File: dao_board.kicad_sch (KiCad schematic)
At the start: 44 parts, among them J1 DISH_LED, J10 KEY6, J11 KEY7, J12 START, J13 SELECT, J14 DISH_SENSOR, J2 USB_C, J3 SWD, J4 GPIO_EXPANSION, J5 KEY1, J6 KEY2, J7 KEY3, J8 KEY4, J9 KEY5, SW1 HX 3x4x2-2P-1.6N, SW2 RESET, U1 MDBT50Q-1MV2, U2 TLC6C598PWR, U3 TLC6C598PWR

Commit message: 回路図の自動アノテーションのやり直し
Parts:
- renumbered C5 to C3, C6 to C4, C3 to C5, C4 to C6, SW2 to SW1, SW1 to SW2
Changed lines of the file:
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@@
 		(dnp no)
 		(fields_autoplaced yes)
-		(property "Reference" "#PWR07"
+		(property "Reference" "#PWR06"
 			(at 45.72 166.37 0)
 			(hide yes)
@@
 			(project "dao_board"
 				(path "/88e2b3bc-f15b-46e0-bc23-bfcd5e24d1de"
-					(reference "#PWR07")
+					(reference "#PWR06")
 					(unit 1)
 				)
@@
 		(dnp no)
 		(fields_autoplaced yes)
-		(property "Reference" "#PWR021"
+		(property "Reference" "#PWR027"
 			(at 247.65 87.63 0)
 			(hide yes)
@@
 			(project "dao_board"
 				(path "/88e2b3bc-f15b-46e0-bc23-bfcd5e24d1de"
-					(reference "#PWR021")
+					(reference "#PWR027")
 					(unit 1)
 				)
@@
 		(in_pos_files yes)
 		(dnp no)
-		(property "Reference" "C5"
+		(property "Reference" "C3"
 			(at 191.008 101.854 90)
 			(show_name no)
@@
 			(project "dao_board"
 				(path "/88e2b3bc-f15b-46e0-bc23-bfcd5e24d1de"
-					(reference "C5")
+					(reference "C3")
 					(unit 1)
 				)
@@
 		(dnp no)
 		(fields_autoplaced yes)
-		(property "Reference" "#PWR025"
+		(property "Reference" "#PWR024"
 			(at 238.76 109.22 0)
 			(hide yes)
@@
 			(project "dao_board"
 				(path "/88e2b3bc-f15b-46e0-bc23-bfcd5e24d1de"
-					(reference "#PWR025")
+					(reference "#PWR024")
 					(unit 1)
 				)
@@
 		(dnp no)
 		(fields_autoplaced yes)
-		(property "Reference" "SW1"
+		(property "Reference" "SW2"
 			(at 63.5 63.1825 0)
 			(show_name no)
@@
 			(project "dao_board"
 				(path "/88e2b3bc-f15b-46e0-bc23-bfcd5e24d1de"
-					(reference "SW1")
+					(reference "SW2")
 					(unit 1)
 				)
@@
 		(dnp no)
 		(fields_autoplaced yes)
-		(property "Reference" "#PWR05"
+		(property "Reference" "#PWR011"
 			(at 74.93 71.12 0)
 			(hide yes)
@@
 			(project "dao_board"
 				(path "/88e2b3bc-f15b-46e0-bc23-bfcd5e24d1de"
-					(reference "#PWR05")
+					(reference "#PWR011")
 					(unit 1)
 				)
@@
 		(dnp no)
 		(fields_autoplaced yes)
-		(property "Reference" "#PWR027"
+		(property "Reference" "#PWR021"
 			(at 173.99 102.87 0)
 			(hide yes)
@@
 			(project "dao_board"
 				(path "/88e2b3bc-f15b-46e0-bc23-bfcd5e24d1de"
-					(reference "#PWR027")
+					(reference "#PWR021")
 					(unit 1)
 				)
@@
 		(dnp no)
 		(fields_autoplaced yes)
-		(property "Reference" "#PWR029"
+		(property "Reference" "#PWR019"
 			(at 172.72 127 0)
 			(hide yes)
@@
 			(project "dao_board"
 				(path "/88e2b3bc-f15b-46e0-bc23-bfcd5e24d1de"
-					(reference "#PWR029")
+					(reference "#PWR019")
 					(unit 1)
 				)
@@
 		(in_pos_files yes)
 		(dnp no)
-		(property "Reference" "C4"
+		(property "Reference" "C6"
 			(at 237.49 96.774 90)
 			(show_name no)
@@
 			(project "dao_board"
 				(path "/88e2b3bc-f15b-46e0-bc23-bfcd5e24d1de"
-					(reference "C4")
+					(reference "C6")
 					(unit 1)
 				)
@@
 		(dnp no)
 		(fields_autoplaced yes)
-		(property "Reference" "#PWR024"
+		(property "Reference" "#PWR030"
 			(at 265.43 78.74 0)
 			(hide yes)
@@
 			(project "dao_board"
 				(path "/88e2b3bc-f15b-46e0-bc23-bfcd5e24d1de"
-					(reference "#PWR024")
+					(reference "#PWR030")
 					(unit 1)
 				)
@@
 		(dnp no)
 		(fields_autoplaced yes)
-		(property "Reference" "C3"
+		(property "Reference" "C5"
 			(at 237.49 80.01 90)
 			(show_name no)
@@
 			(project "dao_board"
 				(path "/88e2b3bc-f15b-46e0-bc23-bfcd5e24d1de"
-					(reference "C3")
+					(reference "C5")
 					(unit 1)
 				)
@@
 		(dnp no)
 		(fields_autoplaced yes)
-		(property "Reference" "#PWR012"
+		(property "Reference" "#PWR07"
 			(at 50.8 111.76 0)
 			(hide yes)
@@
 			(project "dao_board"
 				(path "/88e2b3bc-f15b-46e0-bc23-bfcd5e24d1de"
-					(reference "#PWR012")
+					(reference "#PWR07")
 					(unit 1)
 				)
@@
 		(dnp no)
 		(fields_autoplaced yes)
-		(property "Reference" "#PWR022"
+		(property "Reference" "#PWR028"
 			(at 247.65 92.71 0)
 			(hide yes)
@@
 			(project "dao_board"
 				(path "/88e2b3bc-f15b-46e0-bc23-bfcd5e24d1de"
-					(reference "#PWR022")
+					(reference "#PWR028")
 					(unit 1)
 				)
@@
 		(dnp no)
 		(fields_autoplaced yes)
-		(property "Reference" "#PWR020"
+		(property "Reference" "#PWR026"
 			(at 241.3 54.61 0)
 			(hide yes)
@@
 			(project "dao_board"
 				(path "/88e2b3bc-f15b-46e0-bc23-bfcd5e24d1de"
-					(reference "#PWR020")
+					(reference "#PWR026")
 					(unit 1)
 				)
@@
 		(dnp no)
 		(fields_autoplaced yes)
-		(property "Reference" "#PWR06"
+		(property "Reference" "#PWR05"
 			(at 41.91 148.59 0)
 			(hide yes)
@@
 			(project "dao_board"
 				(path "/88e2b3bc-f15b-46e0-bc23-bfcd5e24d1de"
-					(reference "#PWR06")
+					(reference "#PWR05")
 					(unit 1)
 				)
@@
 		(dnp no)
 		(fields_autoplaced yes)
-		(property "Reference" "#PWR028"
+		(property "Reference" "#PWR022"
 			(at 173.99 134.62 0)
 			(hide yes)
@@
 			(project "dao_board"
 				(path "/88e2b3bc-f15b-46e0-bc23-bfcd5e24d1de"
-					(reference "#PWR028")
+					(reference "#PWR022")
 					(unit 1)
 				)
@@
 		(in_pos_files yes)
 		(dnp no)
-		(property "Reference" "C6"
+		(property "Reference" "C4"
 			(at 191.008 133.858 90)
 			(show_name no)
@@
 			(project "dao_board"
 				(path "/88e2b3bc-f15b-46e0-bc23-bfcd5e24d1de"
-					(reference "C6")
+					(reference "C4")
 					(unit 1)
 				)
@@
 		(dnp no)
 		(fields_autoplaced yes)
-		(property "Reference" "#PWR011"
+		(property "Reference" "#PWR012"
 			(at 69.85 53.34 0)
 			(hide yes)
@@
 			(project "dao_board"
 				(path "/88e2b3bc-f15b-46e0-bc23-bfcd5e24d1de"
-					(reference "#PWR011")
+					(reference "#PWR012")
 					(unit 1)
 				)
@@
 		(dnp no)
 		(fields_autoplaced yes)
-		(property "Reference" "#PWR023"
+		(property "Reference" "#PWR029"
 			(at 275.59 43.18 0)
 			(hide yes)
@@
 			(project "dao_board"
 				(path "/88e2b3bc-f15b-46e0-bc23-bfcd5e24d1de"
-					(reference "#PWR023")
+					(reference "#PWR029")
 					(unit 1)
 				)
@@
 		(dnp no)
 		(fields_autoplaced yes)
-		(property "Reference" "#PWR030"
+		(property "Reference" "#PWR020"
 			(at 172.72 158.75 0)
 			(hide yes)
@@
 			(project "dao_board"
 				(path "/88e2b3bc-f15b-46e0-bc23-bfcd5e24d1de"
-					(reference "#PWR030")
+					(reference "#PWR020")
 					(unit 1)
 				)
@@
 		(dnp no)
 		(fields_autoplaced yes)
-		(property "Reference" "#PWR026"
+		(property "Reference" "#PWR025"
 			(at 238.76 140.97 0)
 			(hide yes)
@@
 			(project "dao_board"
 				(path "/88e2b3bc-f15b-46e0-bc23-bfcd5e24d1de"
-					(reference "#PWR026")
+					(reference "#PWR025")
 					(unit 1)
 				)
@@
 		(dnp no)
 		(fields_autoplaced yes)
-		(property "Reference" "#PWR019"
+		(property "Reference" "#PWR023"
 			(at 223.52 54.61 0)
 			(hide yes)
@@
 			(project "dao_board"
 				(path "/88e2b3bc-f15b-46e0-bc23-bfcd5e24d1de"
-					(reference "#PWR019")
+					(reference "#PWR023")
 					(unit 1)
 				)
@@
 		(dnp no)
 		(fields_autoplaced yes)
-		(property "Reference" "SW2"
+		(property "Reference" "SW1"
 			(at 39.37 104.14 0)
 			(show_name no)
@@
 			(project "dao_board"
 				(path "/88e2b3bc-f15b-46e0-bc23-bfcd5e24d1de"
-					(reference "SW2")
+					(reference "SW1")
 					(unit 1)
 				)

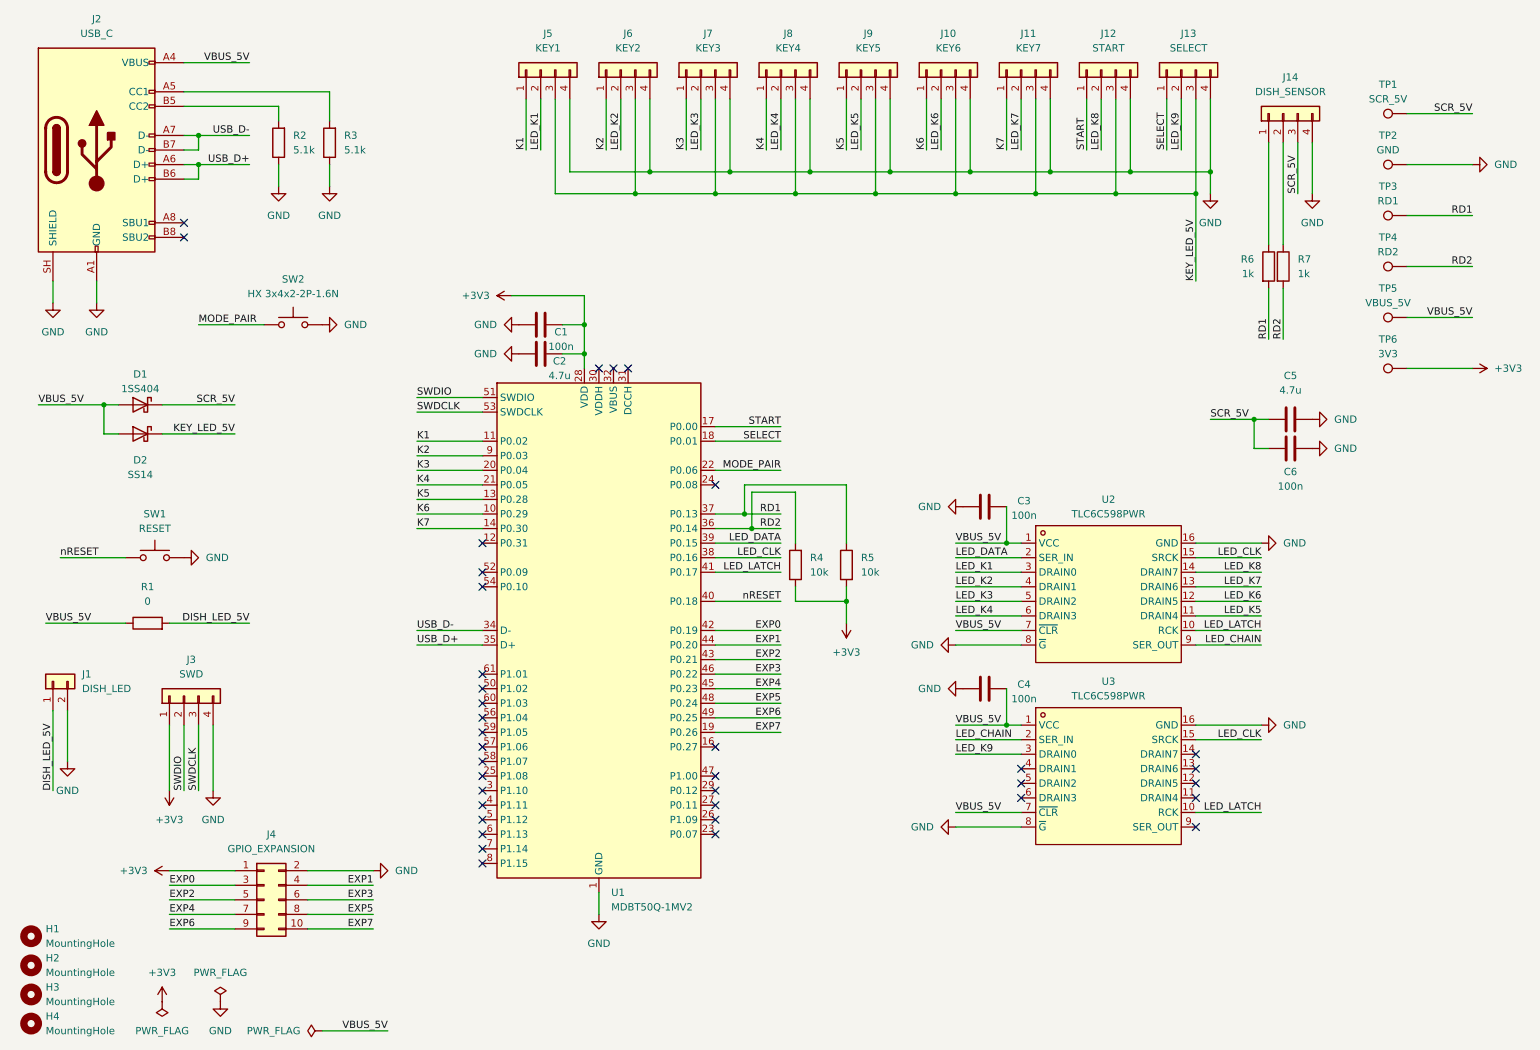
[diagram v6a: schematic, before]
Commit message: USB_Cのシンボルとフットプリントにxiがあったのでシンボル側を適合させた
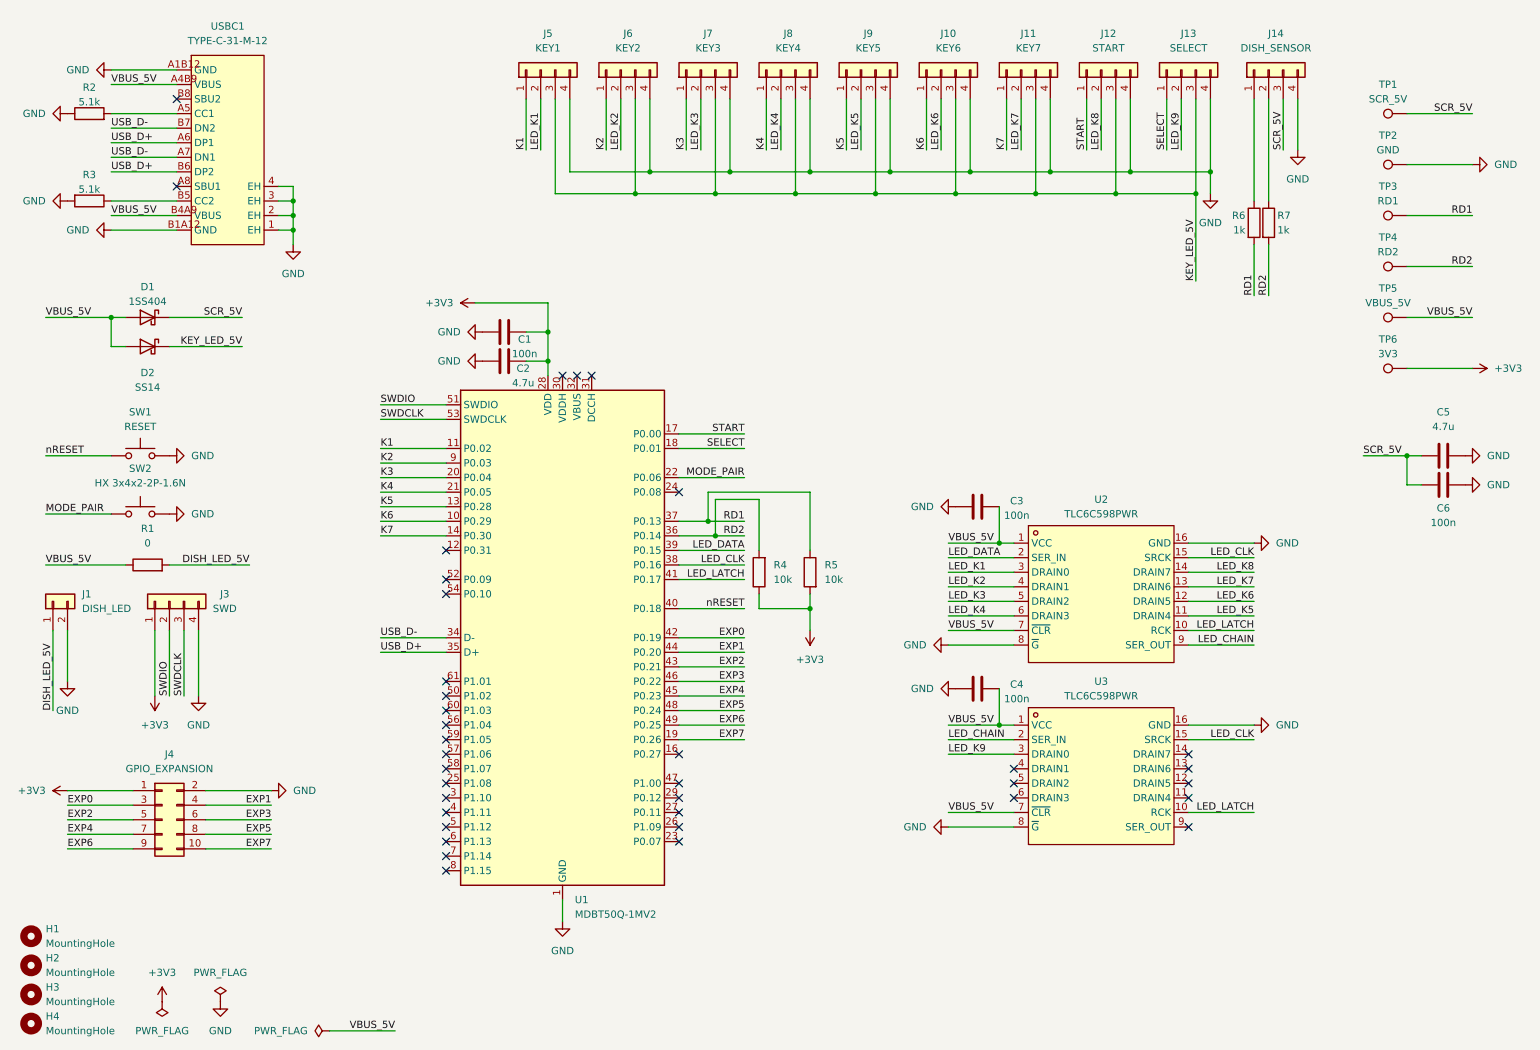
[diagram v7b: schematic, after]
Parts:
- removed J2: USB_C, c165948:USB-C_SMD-TYPE-C-31-M-12_1, symbol Connector:USB_C_Receptacle_USB2.0_16P
- added USBC1: TYPE-C-31-M-12, a:USB-C_SMD-TYPE-C-31-M-12_1, symbol c165948:TYPE-C-31-M-12
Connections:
- net GND: now also R3.2, USBC1.1 (EH), USBC1.2 (EH), USBC1.3 (EH), USBC1.4 (EH), USBC1.A1B12 (GND), USBC1.B1A12 (GND); no longer R3.1
- net USB_D+: now also USBC1.A6 (DP1), USBC1.B6 (DP2)
- net USB_D-: now also USBC1.A7 (DN1), USBC1.B7 (DN2)
- net VBUS_5V: now also USBC1.A4B9 (VBUS), USBC1.B4A9 (VBUS)
- net at R2.2: now also USBC1.A5 (CC1)
- new net: R3.1, USBC1.B5 (CC2)
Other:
- moved on the sheet: C1, C2, C3, C4, C5, C6, D1, D2, J1, J14, J3, J4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

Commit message: フットプリント割り当て忘れてたので割り当て
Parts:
- USBC1: footprint a:USB-C_SMD-TYPE-C-31-M-12_1 -> c165948:USB-C_SMD-TYPE-C-31-M-12_1
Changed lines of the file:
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@@
 			)
 		)
-		(property "Footprint" "a:USB-C_SMD-TYPE-C-31-M-12_1"
+		(property "Footprint" "c165948:USB-C_SMD-TYPE-C-31-M-12_1"
 			(at 49.53 62.23 0)
 			(hide yes)
